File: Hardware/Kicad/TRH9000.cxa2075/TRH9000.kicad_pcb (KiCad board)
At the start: 4 copper layers, 100 x 77.5 mm, 63 parts, among them J1 S-Video, J2 RGB, Q1 BC817, U1 74HC138, U2 74HC32, U3 V9990, U4 KM428C256, U5 KM428C256, U6 CXA2075M, X1 14.31818MHz, Y1 21.47727Mhz

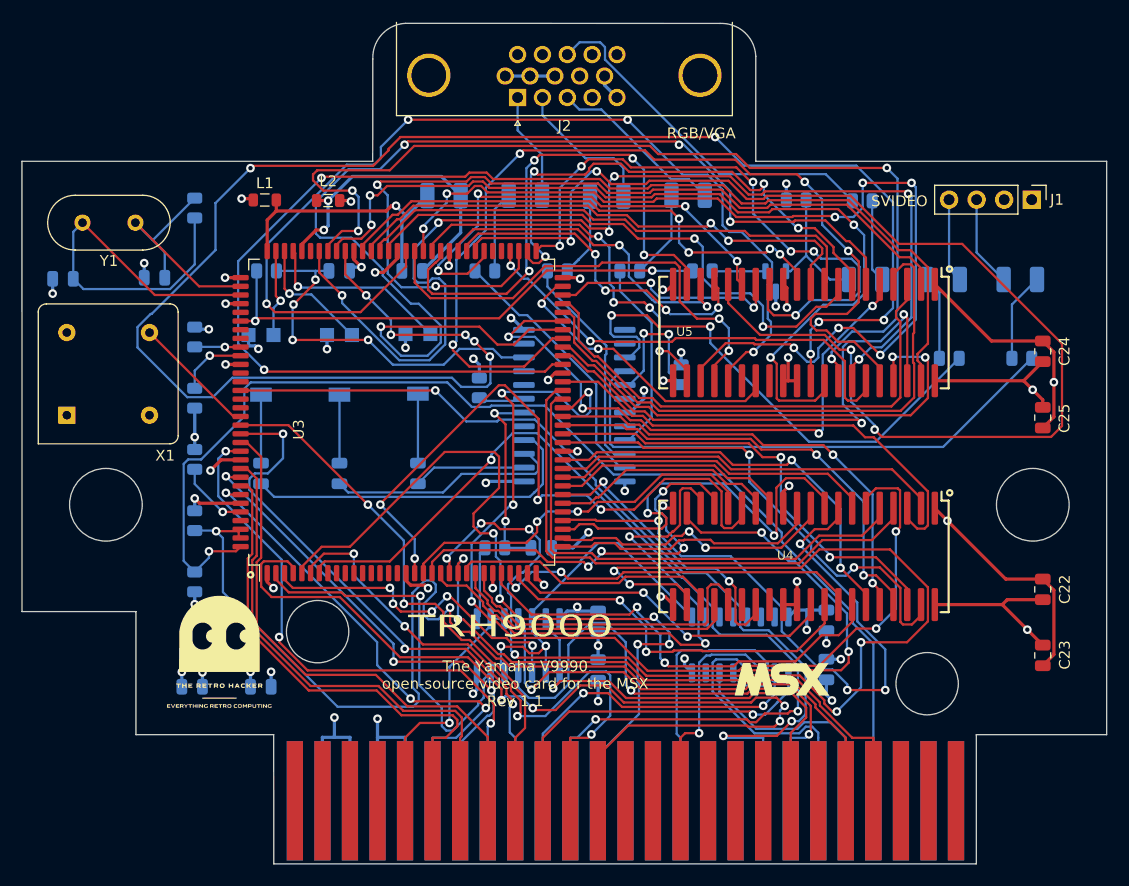
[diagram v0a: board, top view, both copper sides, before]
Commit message: small fix on the YTRAP to use internal for NTSC.
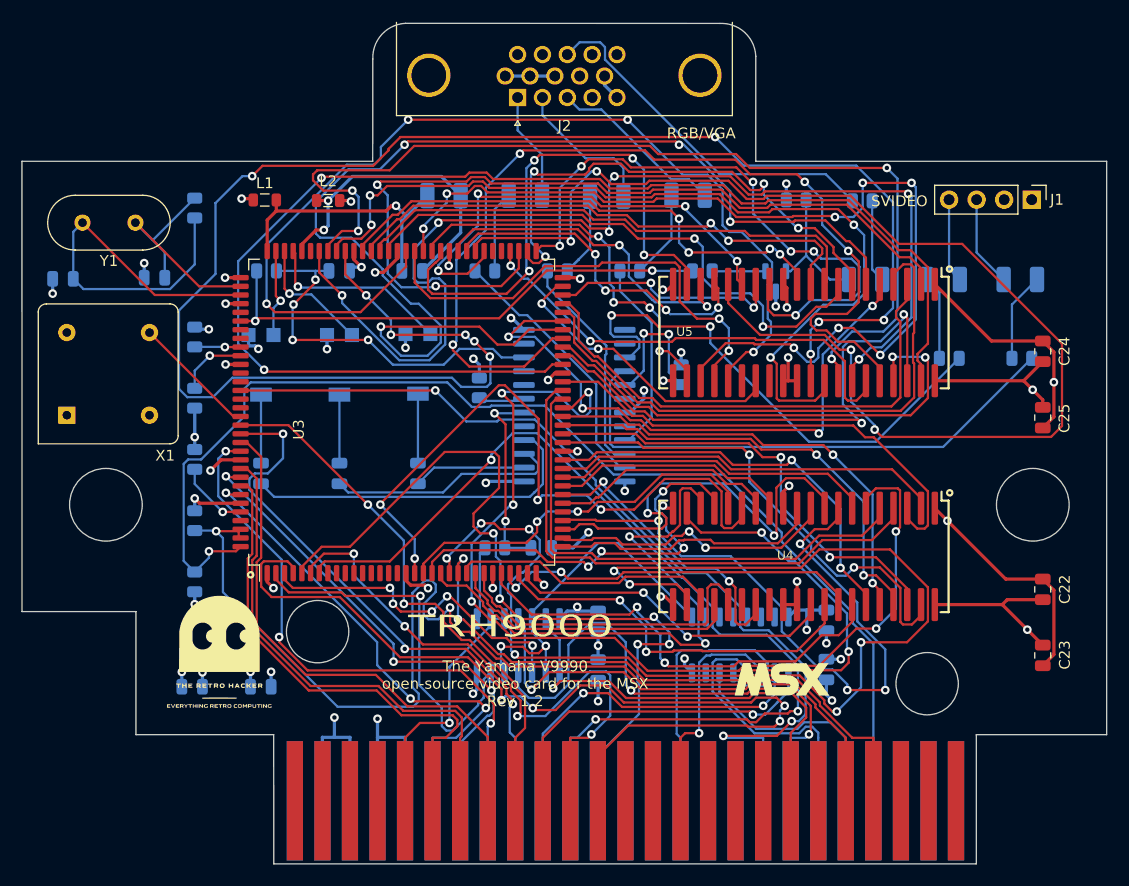
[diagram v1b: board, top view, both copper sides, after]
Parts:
- removed REF**: OSHW-Logo2_24.3x20mm_SilkScreen, Symbol:OSHW-Logo2_24.3x20mm_SilkScreen
- R13: value 2K61 -> 3K3
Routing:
- net /VDP/V1D4: track 164.5 -> 161.3 mm
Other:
- board text added: "The Yamaha V9990 open-source video card for the MSX Rev 1.2"
- board text removed: "The Yamaha V9990 open-source video card for the MSX Rev 1.1"
